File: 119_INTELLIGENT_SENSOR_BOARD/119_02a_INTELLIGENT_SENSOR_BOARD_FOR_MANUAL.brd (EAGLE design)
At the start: 14.6 x 37.5 mm, 14 parts

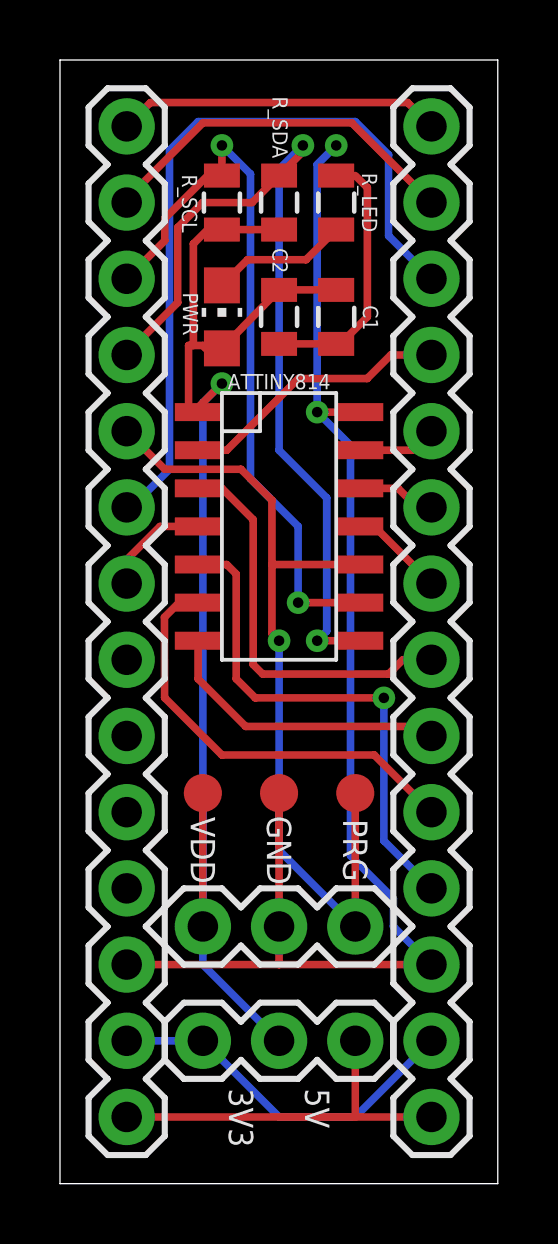
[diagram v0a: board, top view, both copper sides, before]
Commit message: Formed new documentation
Split manual into datasheet, library and notes... added a few more ISC library header defines
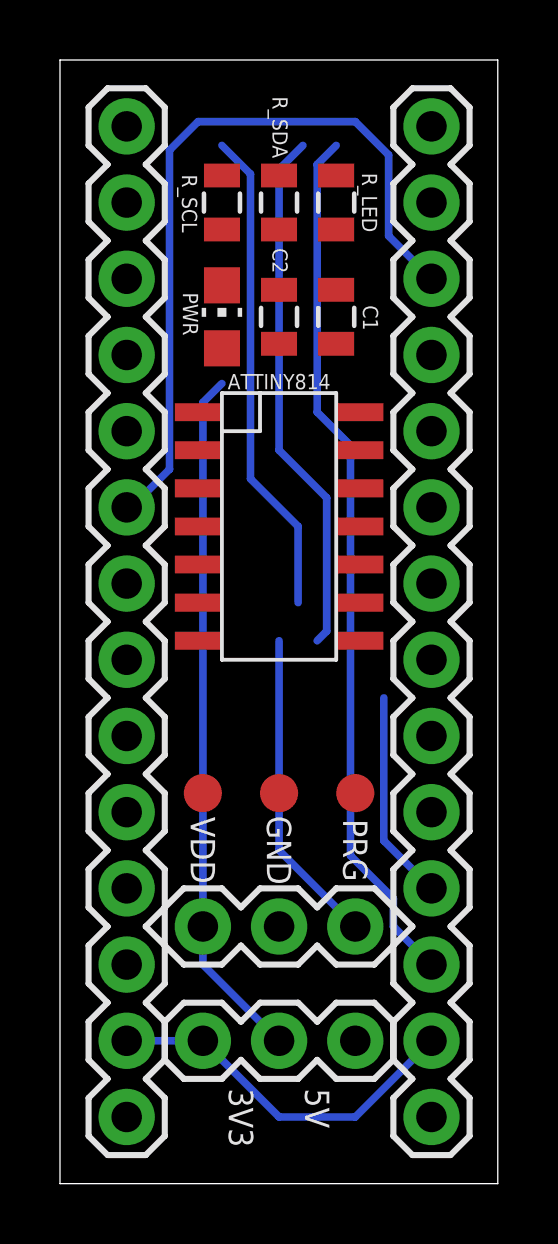
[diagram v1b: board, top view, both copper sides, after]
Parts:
- C1: value 0.1u -> (none)
- C2: value 3.3u -> (none)
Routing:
- net GND: track 54.6 -> 29.1 mm, vias 2 -> 0
- net VDD: track 43.7 -> 23.2 mm, vias 1 -> 0
- net UPDI: track 28.5 -> 10.6 mm, vias 1 -> 0
- net D12: track 14.5 -> 0.00 mm
- net A0: track 13.4 -> 0.00 mm
- net 3V3: track 12.7 -> 0.00 mm
- net [GND]: track 12.4 -> 0.00 mm
- net SDA: track 29.4 -> 17.6 mm, vias 2 -> 0
- net [5V]: track 10.8 -> 0.00 mm
- net D6: track 17.1 -> 7.01 mm, vias 1 -> 0
- net D11: track 9.84 -> 0.00 mm
- net A4: track 9.10 -> 0.00 mm
- net SCL: track 24.4 -> 16.3 mm, vias 2 -> 0
- net N$1: track 4.58 -> 0.00 mm
- net INTERRUPT: track 3.63 -> 0.00 mm
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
